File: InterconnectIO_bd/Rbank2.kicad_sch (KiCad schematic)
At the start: 48 parts, among them K24 TQ2-5, K25 TQ2-5, K26 TQ2-5, K27 TQ2-5, K28 TQ2-5, K29 TQ2-5, K30 TQ2-5, K31 TQ2-5, K32 TQ2-5

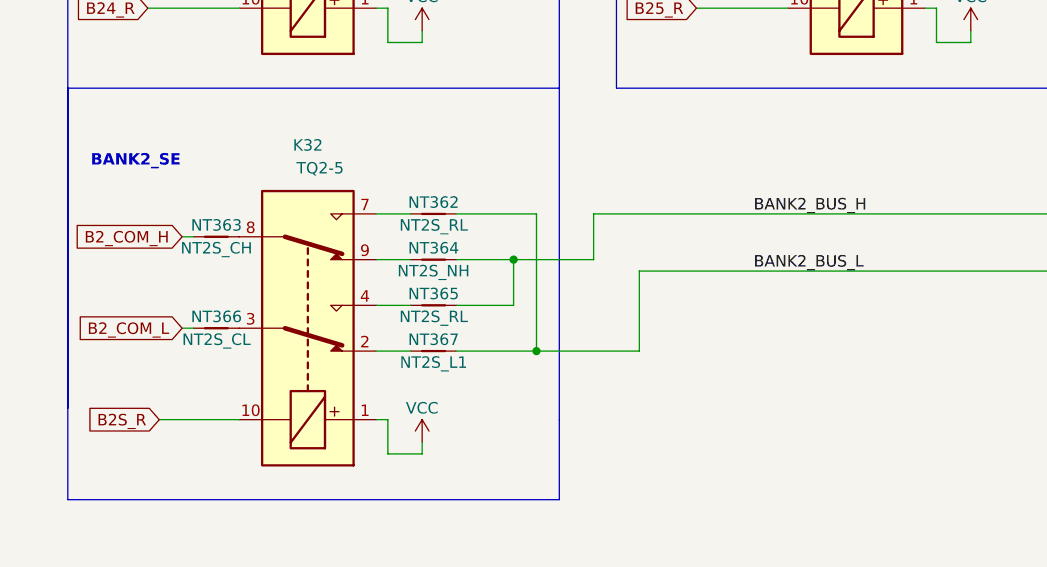
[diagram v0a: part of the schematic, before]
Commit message: Reverse COM_H and COM_L on relay Bank
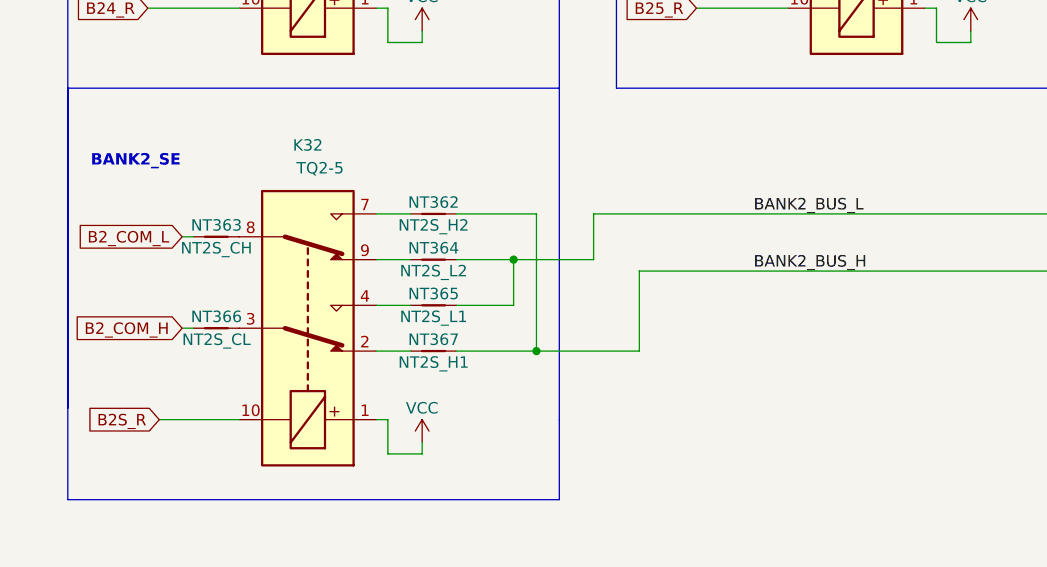
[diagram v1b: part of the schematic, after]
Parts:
- NT362: value NT2S_RL -> NT2S_H2
- NT364: value NT2S_NH -> NT2S_L2
- NT365: value NT2S_RL -> NT2S_L1
- NT367: value NT2S_L1 -> NT2S_H1
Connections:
- net B2_COM_H: now also NT366.1; no longer NT363.1
- net B2_COM_L: now also NT363.1; no longer NT366.1
- net BANK2_BUS_H: now also NT349.1, NT354.1, NT355.1, NT356.1, NT357.1, NT362.2, NT367.2, NT45.1, NT46.1, NT47.1; no longer NT350.1, NT351.1, NT352.1, NT353.1, NT358.1, NT359.1, NT360.1, NT361.1, NT364.2, NT365.2
- net BANK2_BUS_L: now also NT350.1, NT351.1, NT352.1, NT353.1, NT358.1, NT359.1, NT360.1, NT361.1, NT364.2, NT365.2; no longer NT349.1, NT354.1, NT355.1, NT356.1, NT357.1, NT362.2, NT367.2, NT45.1, NT46.1, NT47.1
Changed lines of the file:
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@@
     (effects (font (size 1.27 1.27)) (justify left bottom))
   )
-  (label "BANK2_BUS_L" (at 96.52 129.54 0) (fields_autoplaced)
+  (label "BANK2_BUS_H" (at 96.52 129.54 0) (fields_autoplaced)
     (effects (font (size 1.27 1.27)) (justify left bottom))
   )
@@
     (effects (font (size 1.27 1.27)) (justify left bottom))
   )
-  (label "BANK2_BUS_H" (at 96.52 123.19 0) (fields_autoplaced)
+  (label "BANK2_BUS_L" (at 96.52 123.19 0) (fields_autoplaced)
     (effects (font (size 1.27 1.27)) (justify left bottom))
   )
@@
     )
   )
-  (global_label "B2_COM_H" (shape input) (at 33.02 125.73 180) (fields_autoplaced)
+  (global_label "B2_COM_L" (shape input) (at 33.02 125.73 180) (fields_autoplaced)
     (effects (font (size 1.27 1.27)) (justify right))
-    (property "Intersheetrefs" "${INTERSHEET_REFS}" (at 20.8098 125.6506 0)
+    (property "Intersheetrefs" "${INTERSHEET_REFS}" (at 20.6195 125.73 0)
       (effects (font (size 1.27 1.27)) (justify right) hide)
     )
@@
     )
   )
-  (global_label "B2_COM_L" (shape input) (at 33.02 135.89 180) (fields_autoplaced)
+  (global_label "B2_COM_H" (shape input) (at 33.02 135.89 180) (fields_autoplaced)
     (effects (font (size 1.27 1.27)) (justify right))
-    (property "Intersheetrefs" "${INTERSHEET_REFS}" (at 21.1121 135.8106 0)
+    (property "Intersheetrefs" "${INTERSHEET_REFS}" (at 20.3171 135.89 0)
       (effects (font (size 1.27 1.27)) (justify right) hide)
     )
@@
       (effects (font (size 1.27 1.27)))
     )
-    (property "Value" "NT2S_NH" (at 60.96 129.54 0)
+    (property "Value" "NT2S_L2" (at 60.96 129.54 0)
       (effects (font (size 1.27 1.27)))
     )
@@
       (effects (font (size 1.27 1.27)))
     )
-    (property "Value" "NT2S_RL" (at 60.96 124.46 0)
+    (property "Value" "NT2S_H2" (at 60.96 124.46 0)
       (effects (font (size 1.27 1.27)))
     )
@@
       (effects (font (size 1.27 1.27)))
     )
-    (property "Value" "NT2S_L1" (at 60.96 139.7 0)
+    (property "Value" "NT2S_H1" (at 60.96 139.7 0)
       (effects (font (size 1.27 1.27)))
     )
@@
       (effects (font (size 1.27 1.27)))
     )
-    (property "Value" "NT2S_RL" (at 60.96 134.62 0)
-      (effects (font (size 1.27 1.27)))
-    )
+    (property "Value" "NT2S_L1" (at 60.96 134.62 0)
+      (effects (font (size 1.27 1.27)))
+    )
